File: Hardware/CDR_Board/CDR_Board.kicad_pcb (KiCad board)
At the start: 2 copper layers, 61 x 40.6 mm, 60 parts, among them J1 nRF52, J2 nRF24, J3 Battery, J4 GPIO & ADC, J5 USB_C_Receptacle_USB2.0, Q1 DMP2045U, SW1 BOOTSEL, SW2 RESET, SW3 SW_SPDT, U1 W25Q32JVSS, U2 AP2112, U3 RP2040, U4 BQ25172, U6 ADXL343, Y1 Crystal

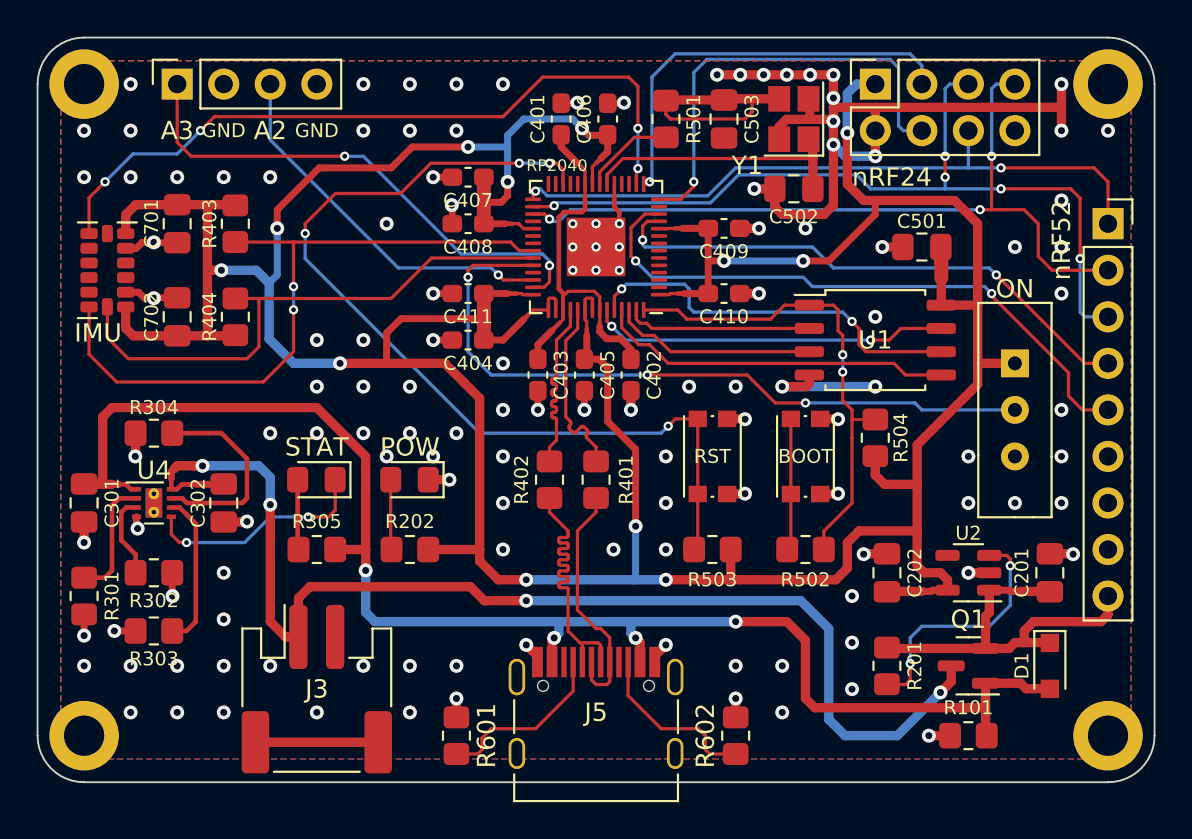
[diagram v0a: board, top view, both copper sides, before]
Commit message: Added pullup/pulldown resistors for IMU
Added pullup resistor for CS, pulldown resistor for ADDR pin of IMU. Moved silkscreen
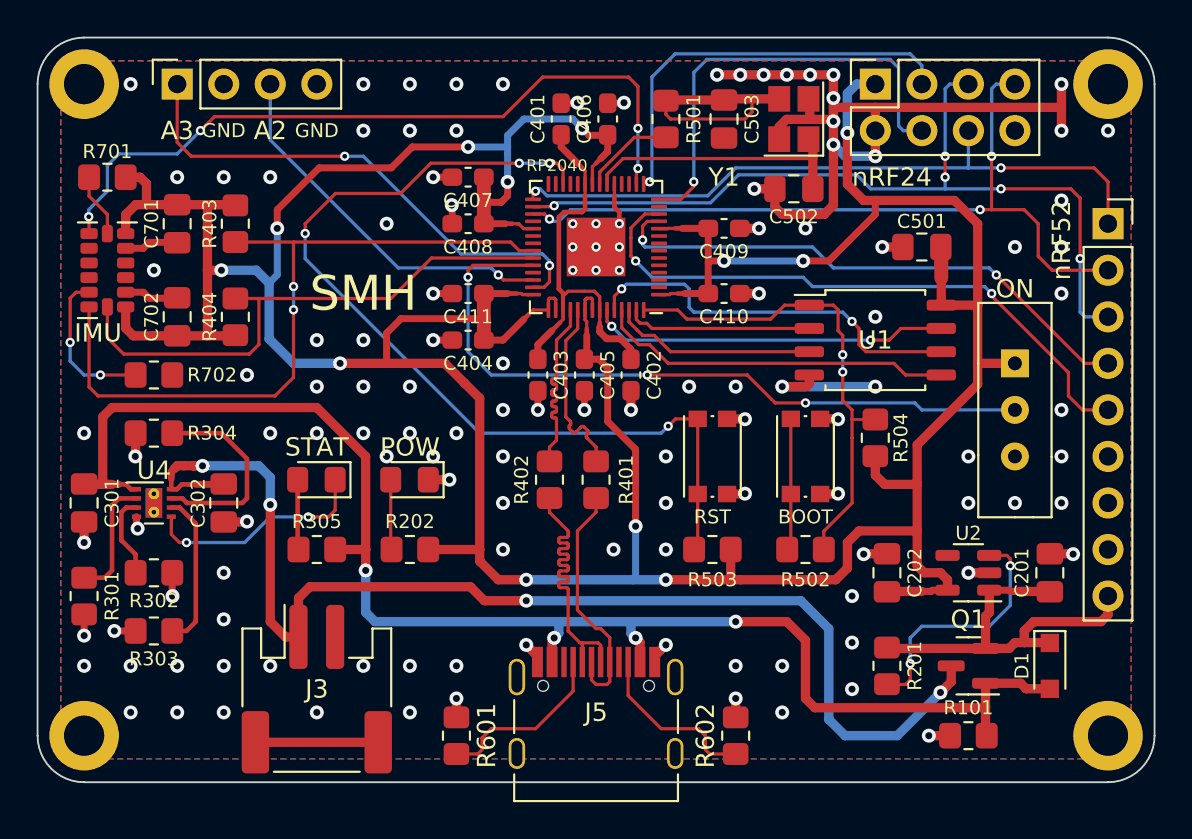
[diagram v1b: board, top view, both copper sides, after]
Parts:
- added R701: 10k, Resistor_SMD:R_0805_2012Metric_Pad1.20x1.40mm_HandSolder, F.Cu at (125.7, 83.8)
- added R702: 10k, Resistor_SMD:R_0805_2012Metric_Pad1.20x1.40mm_HandSolder, F.Cu at (128.3, 94.6)
- R401, R402: value 5K1 -> 1
- R601, R602: value 5K1 -> 5k1
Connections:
- U6 pad 12: unconnected-(U6-Pad12) -> Net-(R702-Pad1)
- U6 pad 7: unconnected-(U6-Pad7) -> Net-(R701-Pad2)
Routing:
- net Net-(R702-Pad1): track 0.00 -> 8.48 mm, vias 0 -> 2
- net Net-(R701-Pad2): track 0.00 -> 3.49 mm
- net /SDA: track 37.5 -> 40.0 mm
- net +3V3: track 226.2 -> 228.6 mm
- net GND: vias 131 -> 128
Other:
- board text added: "SMH"
